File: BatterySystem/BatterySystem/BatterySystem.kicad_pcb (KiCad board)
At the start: 2 copper layers, 30 parts, among them U1 3.3V, U2 BQ25895RTW

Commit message: USB  connectie
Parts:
- moved U2 33.8 mm to (376.7, -38.2)
- moved U3 2.90 mm to (367.5, -37.9)
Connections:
- U3 pad 1: (no net) -> GND
- U3 pad 2: (no net) -> D+
- U3 pad 3: (no net) -> D-
- U3 pad 4: (no net) -> Input
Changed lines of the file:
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@@
   )
   (footprint "Package_DFN_QFN:Texas_S-PWQFN-N24_EP2.7x2.7mm_ThermalVias" (layer "F.Cu")
-    (at 343.015 -41.38)
+    (at 376.6674 -38.1616)
     (descr "QFN, 24 Pin (http://www.ti.com/lit/ds/symlink/bq25601.pdf#page=54), generated with kicad-footprint-generator ipc_noLead_generator.py")
     (tags "QFN NoLead")
@@
   )
   (footprint "VR20S3V3:USB-C 2.0 Female to DIP Adapter" (layer "F.Cu")
-    (at 365.76 -35.56)
+    (at 367.5248 -37.8554)
     (property "Sheetfile" "usb.kicad_sch")
     (property "Sheetname" "USB")
@@
     (fp_line (start 3 7) (end 3 -5)
       (stroke (width 0.12) (type default)) (layer "F.SilkS"))
-    (pad "1" thru_hole circle (at -7.62 5.08) (size 1.524 1.524) (drill 0.762) (layers "*.Cu" "*.Mask"))
-    (pad "2" thru_hole circle (at -5.08 5.08) (size 1.524 1.524) (drill 0.762) (layers "*.Cu" "*.Mask"))
-    (pad "3" thru_hole circle (at -2.54 5.08) (size 1.524 1.524) (drill 0.762) (layers "*.Cu" "*.Mask"))
-    (pad "4" thru_hole circle (at 0 5.08) (size 1.524 1.524) (drill 0.762) (layers "*.Cu" "*.Mask"))
+    (pad "1" thru_hole circle (at -7.62 5.08) (size 1.524 1.524) (drill 0.762) (layers "*.Cu" "*.Mask")
+      (net 2 "GND") (pinfunction "GND") (pintype "passive"))
+    (pad "2" thru_hole circle (at -5.08 5.08) (size 1.524 1.524) (drill 0.762) (layers "*.Cu" "*.Mask")
+      (net 20 "D+") (pinfunction "D+") (pintype "bidirectional"))
+    (pad "3" thru_hole circle (at -2.54 5.08) (size 1.524 1.524) (drill 0.762) (layers "*.Cu" "*.Mask")
+      (net 21 "D-") (pinfunction "D-") (pintype "bidirectional"))
+    (pad "4" thru_hole circle (at 0 5.08) (size 1.524 1.524) (drill 0.762) (layers "*.Cu" "*.Mask")
+      (net 6 "Input") (pinfunction "Vbus") (pintype "power_out"))
   )
 )

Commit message: Beetje gewerkt aan routen van de PCB en positioneren van componenten
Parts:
- moved L2 316.4 mm to (126.9, 114.2), turned to 180 degrees
- moved U3 283.2 mm to (160.0, 154.9), turned to 180 degrees
- moved U2 277.7 mm to (137.9, 103.6), turned to 180 degrees
- moved R6 261.8 mm to (113.5, 110.6)
- moved R7 260.3 mm to (121.2, 101.2), turned to 180 degrees
- moved C6 252.1 mm to (139.6, 112.9), turned to 180 degrees
- moved C10 245.0 mm to (130.8, 107.2), turned to 180 degrees
- moved R1 242.8 mm to (137.1, 99.0), turned to -90 degrees
- moved BT1 242.5 mm to (162.6, 66.0)
- moved C7 242.4 mm to (140.7, 108.4), turned to 180 degrees
- moved R8 241.9 mm to (140.5, 99.0), turned to -90 degrees
- moved C9 241.8 mm to (138.2, 109.1), turned to 90 degrees
- moved C11 241.7 mm to (130.9, 104.0)
- moved C8 241.5 mm to (133.7, 100.1), turned to -90 degrees
- moved R3 241.2 mm to (135.5, 99.0), turned to -90 degrees
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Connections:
- 3V3 pad 1: Net-(U1-Vout) -> Vref
- C5 pad 1: Net-(U1-Vout) -> Vref
- U1 pad 3: Net-(U1-Vout) -> Vref
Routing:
- net Net-(U2-TS): track 0.00 -> 10.4 mm
- net Bat: track 0.00 -> 3.38 mm
- net Net-(U2-INT): track 0.00 -> 2.33 mm
- net Net-(U2-~{CE}): track 0.00 -> 2.04 mm
- net Net-(U2-ILIM): track 0.00 -> 2.03 mm
- net GND: track 0.00 -> 1.91 mm
- net (no net): track 0.00 -> 0.89 mm
- net 3.5-4.5V: track 0.00 -> 0.84 mm
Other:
- board text added: "Made by: A.Benaissa and N.Ganga"

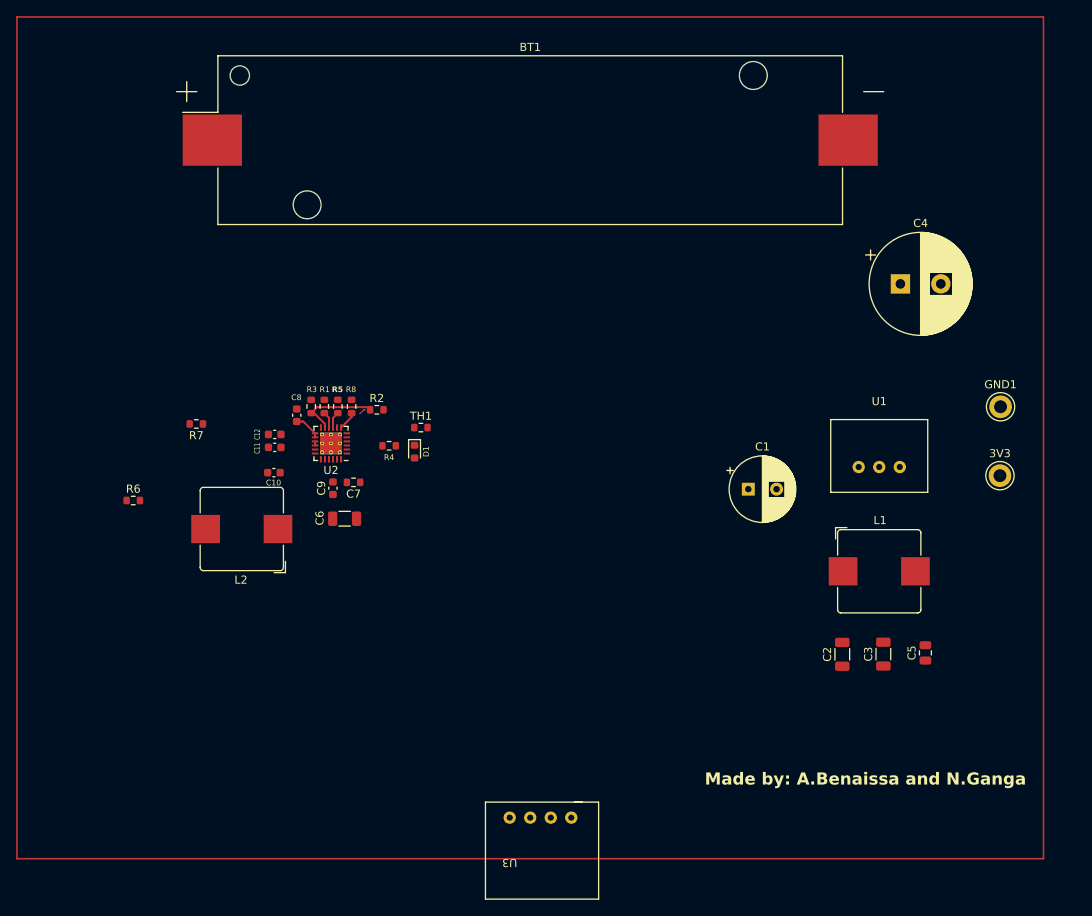
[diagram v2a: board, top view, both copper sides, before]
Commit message: Traces toegevoegd
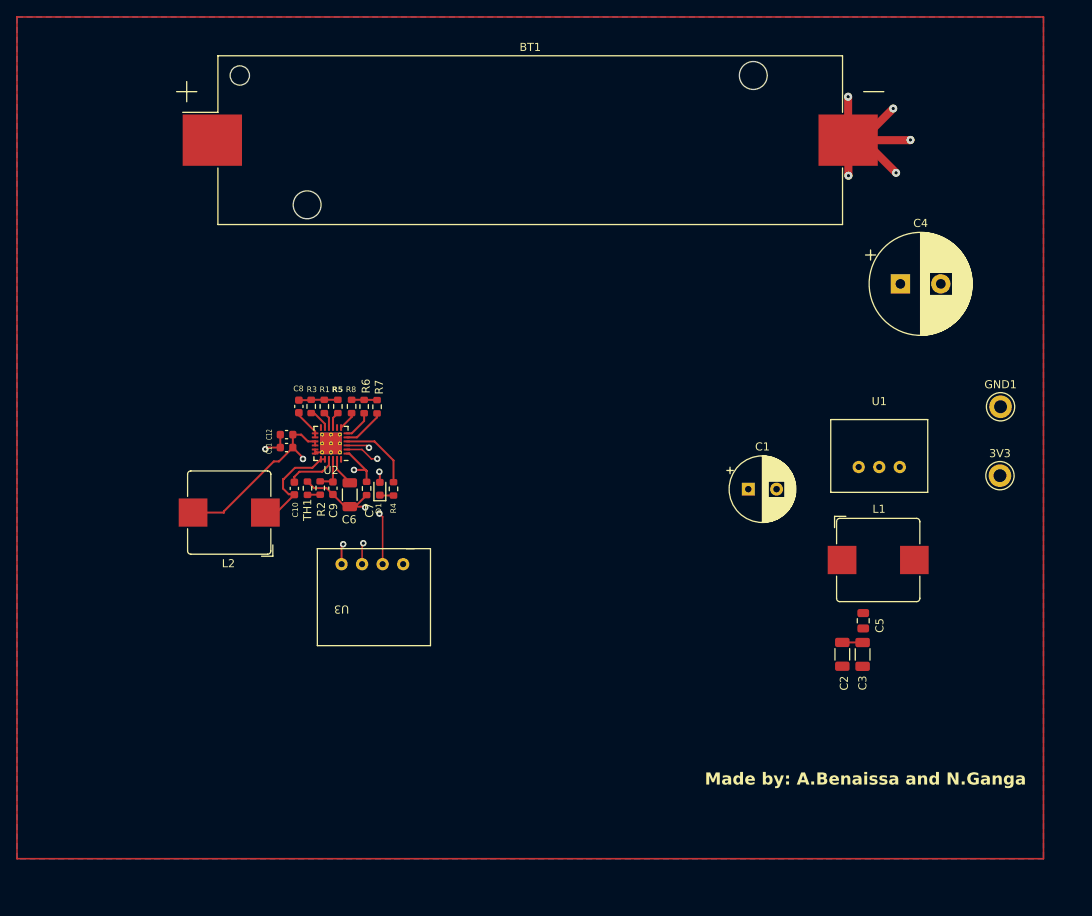
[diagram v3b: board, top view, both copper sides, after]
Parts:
- moved U3 37.6 mm to (139.2, 123.6)
- moved R6 30.8 mm to (142.0, 99.0), turned to -90 degrees
- moved R7 22.5 mm to (143.6, 99.0), turned to -90 degrees
- moved TH1 15.9 mm to (135.0, 109.1), turned to 90 degrees
- moved R2 11.9 mm to (136.6, 109.1), turned to 90 degrees
- moved C5 8.66 mm to (203.8, 125.5), turned to -90 degrees
- moved D1 6.29 mm to (144.0, 109.2), turned to 90 degrees
- moved R4 5.36 mm to (145.6, 109.2), turned to 90 degrees
- moved C10 3.19 mm to (133.4, 109.1), turned to -90 degrees
- moved C6 3.03 mm to (140.2, 109.9), turned to -90 degrees
- moved C3 2.57 mm to (203.7, 129.7)
- moved L2 2.56 mm to (125.3, 112.1)
- moved C7 1.78 mm to (142.3, 109.1), turned to -90 degrees
- moved C11 1.46 mm to (132.4, 104.1)
- moved C12 1.46 mm to (132.4, 102.5)
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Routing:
- net GND: track 1.91 -> 57.8 mm, vias 0 -> 7
- net 3.5-4.5V: track 0.84 -> 34.7 mm, vias 0 -> 2
- net D-: track 0.00 -> 20.2 mm, vias 0 -> 2
- net Input: track 0.00 -> 18.6 mm, vias 0 -> 2
- net D+: track 0.00 -> 18.4 mm, vias 0 -> 2
- net Net-(C10-Pad2): track 0.00 -> 13.6 mm
- net Net-(U2-STAT): track 0.00 -> 9.44 mm
- net Net-(U2-BTST): track 0.00 -> 6.26 mm
- net Net-(U2-TS): track 10.4 -> 4.30 mm
- net Net-(U2-SCL): track 0.00 -> 5.25 mm
- net Net-(U2-REGN): track 0.00 -> 4.41 mm
- net Net-(U2-SDA): track 0.00 -> 3.74 mm
- net Phone: track 0.00 -> 3.56 mm
- net Vref: track 0.00 -> 3.17 mm
- net Net-(D1-K): track 0.00 -> 1.71 mm
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- added copper zone on B.Cu, net GND
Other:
- copper layers 2 -> 4

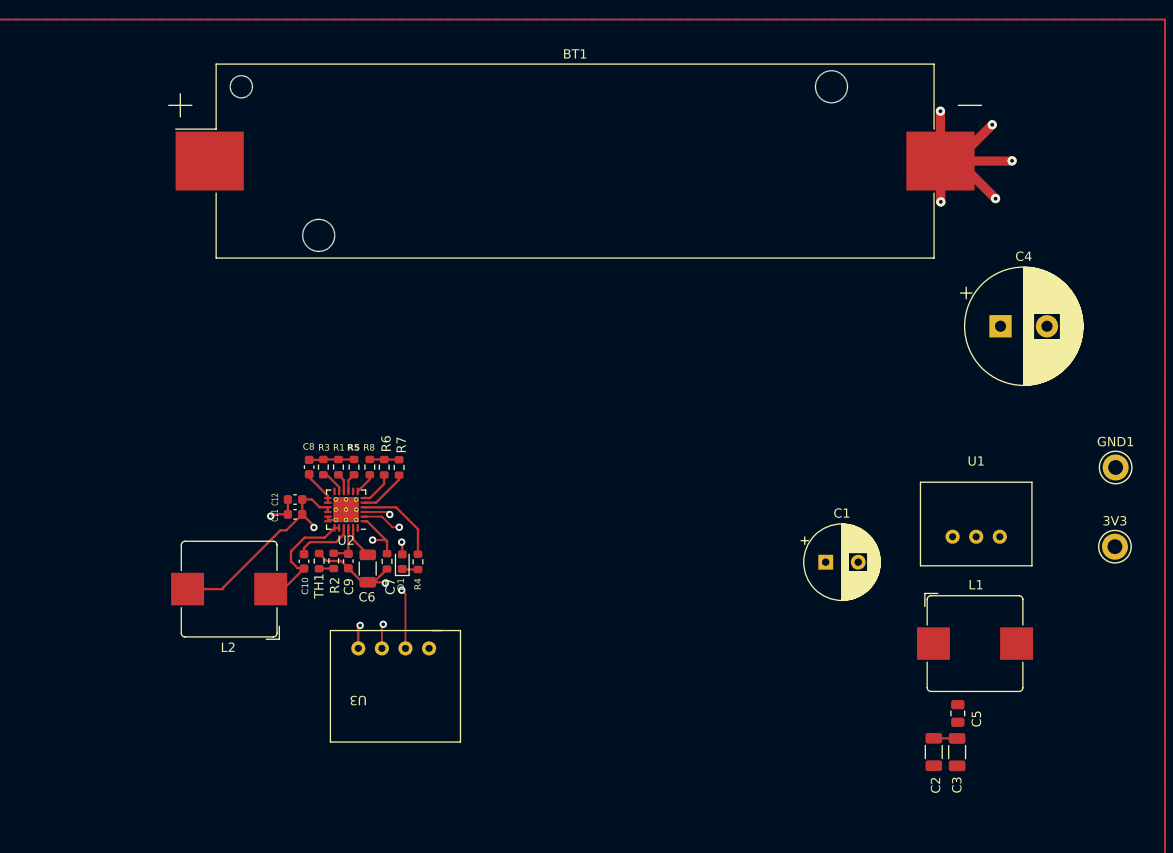
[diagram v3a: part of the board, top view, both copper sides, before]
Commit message: Buck converter gedaan en meer test point toegevoegd
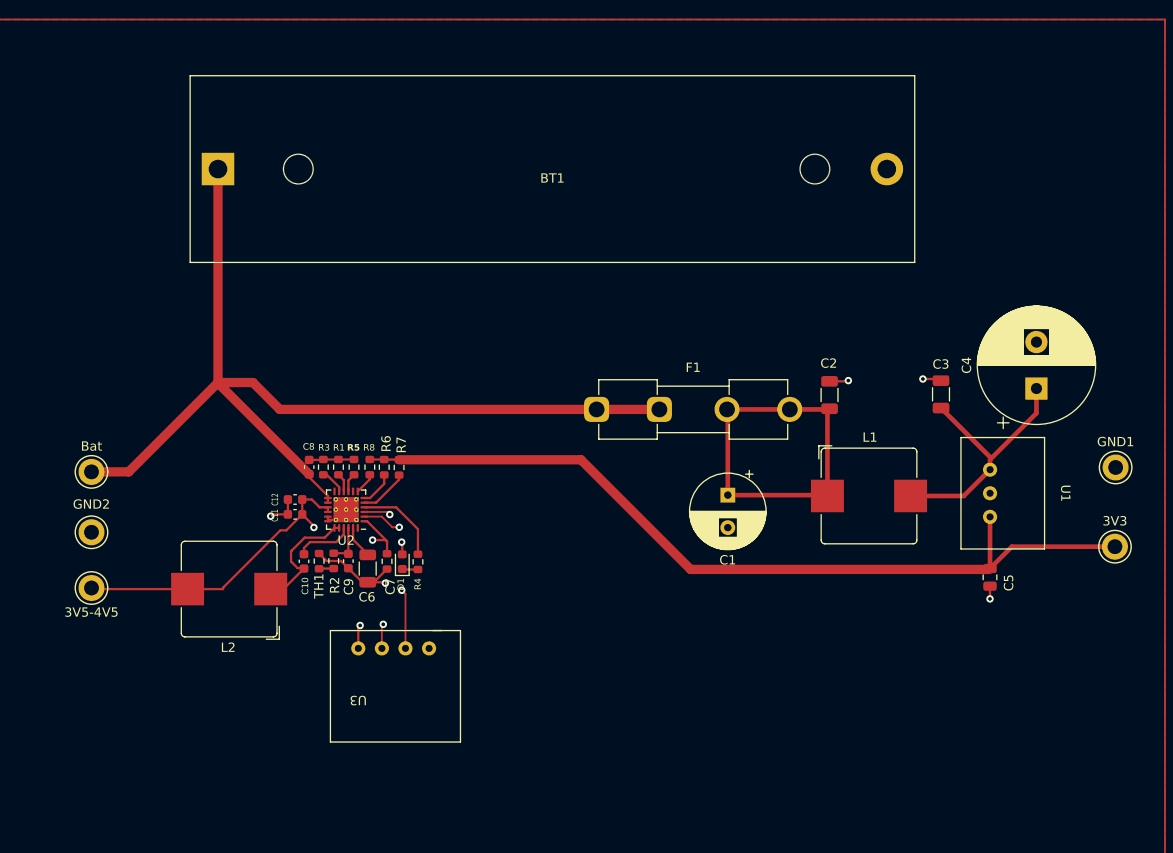
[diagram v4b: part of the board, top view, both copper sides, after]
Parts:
- added 3V5-4V5: TestPoint, TestPoint:TestPoint_Keystone_5005-5009_Compact, F.Cu at (110.5, 112.0)
- added Bat: TestPoint, TestPoint:TestPoint_Keystone_5005-5009_Compact, F.Cu at (110.5, 99.5)
- added F1: Fuse, Fuse:Fuseholder_Clip-5x20mm_Eaton_1A5601-01_Inline_P20.80x6.76mm_D1.70mm_Horizontal, F.Cu at (164.9, 92.8)
- added GND2: TestPoint, TestPoint:TestPoint_Keystone_5005-5009_Compact, F.Cu at (110.5, 106.0)
- BT1: footprint Battery:BatteryHolder_Keystone_1042_1x18650 -> Battery:BatteryHolder_MPD_BH-18650-PC2
- moved C2 40.0 mm to (189.9, 91.2)
- moved C3 38.6 mm to (201.9, 91.2)
- moved BT1 38.4 mm to (124.1, 66.9)
- moved L1 19.6 mm to (194.2, 102.1)
- moved C5 15.1 mm to (207.2, 110.8)
- moved C1 12.8 mm to (179.0, 102.0), turned to -90 degrees
- moved U1 9.57 mm to (214.8, 101.8), turned to -90 degrees
- moved C4 7.74 mm to (212.2, 90.5), turned to 90 degrees
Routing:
- net Bat: track 3.89 -> 107.1 mm
- net Vref: track 3.17 -> 91.7 mm
- net Net-(C1-Pad1): track 0.00 -> 40.6 mm
- net GND: track 57.8 -> 28.3 mm, vias 7 -> 5
- net Net-(U1-Vin): track 0.00 -> 28.3 mm
- net 3.5-4.5V: track 34.7 -> 45.1 mm

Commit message: PCB tracing afgemaakt
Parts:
- moved C4 57.8 mm to (161.4, 118.2), turned to 180 degrees
- moved 3V3 43.3 mm to (180.5, 123.6)
- moved GND1 41.4 mm to (187.3, 123.4)
- moved C5 32.9 mm to (175.0, 117.4)
- moved U1 26.6 mm to (190.6, 112.7)
- moved C1 24.5 mm to (154.5, 103.0)
- moved L1 23.9 mm to (170.6, 105.9)
- moved C3 22.8 mm to (179.2, 92.4)
- moved F1 14.9 mm to (150.0, 91.6)
- moved C2 13.4 mm to (176.6, 92.4)
- moved BT1 12.6 mm to (114.7, 75.2)
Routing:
- net Net-(U2-TS): track 4.30 -> 27.2 mm, vias 0 -> 2
- net Net-(U1-Vin): track 28.3 -> 42.0 mm
- net Vref: track 91.7 -> 78.3 mm
- net Bat: track 107.1 -> 96.4 mm
- net GND: track 28.3 -> 36.2 mm
- net Net-(C1-Pad1): track 40.6 -> 41.9 mm
- added copper zone on In1.Cu, net GND
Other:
- board outline added: 84.1 x 65 mm

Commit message: Tracing afgemaakt
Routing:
- net GND: track 36.2 -> 43.7 mm
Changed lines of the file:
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@@
   (segment (start 139.6576 111.3826) (end 138.15 109.875) (width 0.25) (layer "F.Cu") (net 2))
   (segment (start 129.9883 104.0727) (end 129.794 104.267) (width 0.25) (layer "F.Cu") (net 2))
-  (segment (start 136.81 102.4625) (end 137.91 103.5625) (width 0.25) (layer "F.Cu") (net 2))
   (segment (start 140.7704 111.3826) (end 141.4018 112.014) (width 0.25) (layer "F.Cu") (net 2))
   (segment (start 137.36 109.09) (end 135.8108 109.09) (width 0.25) (layer "F.Cu") (net 2))
@@
   (via (at 141.4018 113.0554) (size 0.8) (drill 0.4) (layers "F.Cu" "B.Cu") (net 2))
   (via (at 175.0314 119.761) (size 0.8) (drill 0.4) (layers "F.Cu" "B.Cu") (net 2))
+  (segment (start 139.01 102.4625) (end 137.91 103.5625) (width 0.25) (layer "B.Cu") (net 2))
+  (segment (start 137.91 102.4625) (end 137.91 103.5625) (width 0.25) (layer "B.Cu") (net 2))
+  (segment (start 139.01 103.5625) (end 137.91 103.5625) (width 0.25) (layer "B.Cu") (net 2))
+  (segment (start 139.01 104.6625) (end 137.91 103.5625) (width 0.25) (layer "B.Cu") (net 2))
   (segment (start 139.01 104.6625) (end 137.91 104.6625) (width 0.25) (layer "B.Cu") (net 2))
-  (segment (start 139.01 102.4625) (end 137.91 103.5625) (width 0.25) (layer "B.Cu") (net 2))
+  (segment (start 137.91 104.6625) (end 137.91 103.5625) (width 0.25) (layer "B.Cu") (net 2))
+  (segment (start 136.81 103.5625) (end 137.91 103.5625) (width 0.25) (layer "B.Cu") (net 2))
+  (segment (start 136.81 102.4625) (end 137.91 103.5625) (width 0.25) (layer "B.Cu") (net 2))
+  (segment (start 136.81 104.6625) (end 137.91 103.5625) (width 0.25) (layer "B.Cu") (net 2))
   (segment (start 176.5566 93.9534) (end 176.6316 93.8784) (width 0.25) (layer "F.Cu") (net 3))
   (segment (start 164.041 103.7714) (end 166.1368 105.8672) (width 0.25) (layer "F.Cu") (net 3))
